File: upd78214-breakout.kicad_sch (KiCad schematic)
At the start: 26 parts, among them J1 Conn_02x17_Odd_Even, U1 upd78214-64p-qfp, X1 USB-B1HSB6

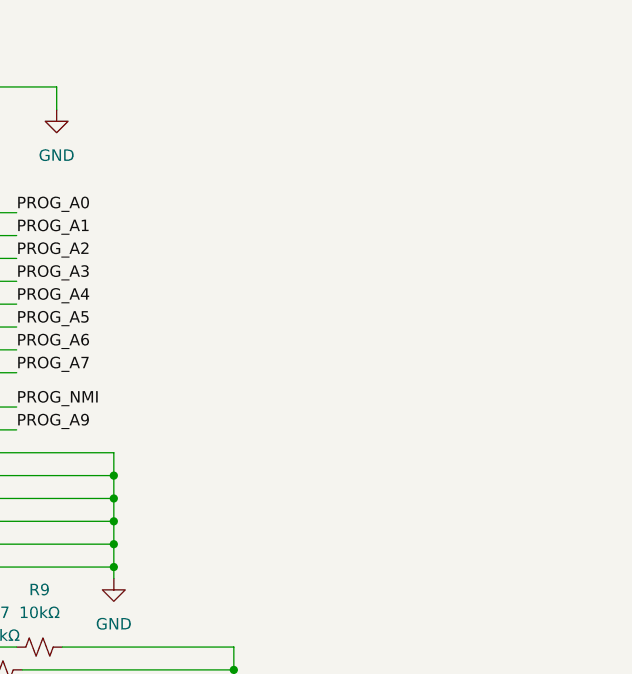
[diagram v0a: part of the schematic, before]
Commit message: 12V injection hooks
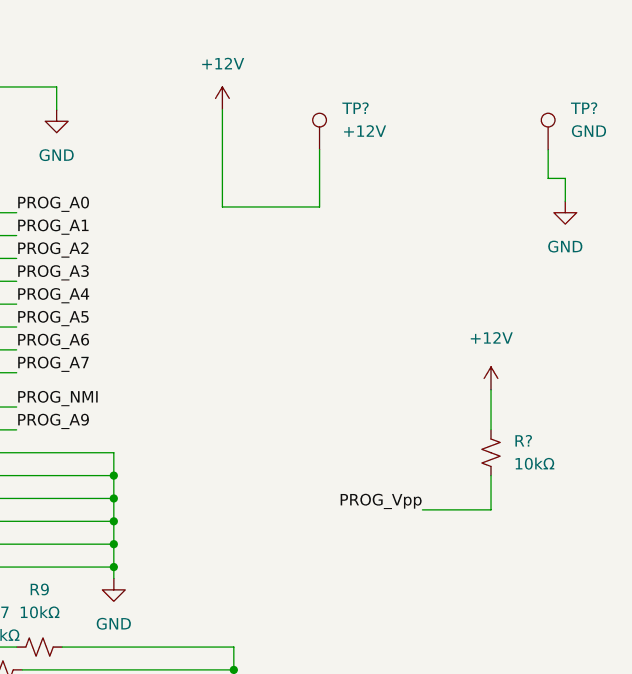
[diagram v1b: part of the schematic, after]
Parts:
- added R?: 10kΩ, Resistor_THT:R_Axial_DIN0207_L6.3mm_D2.5mm_P10.16mm_Horizontal, symbol Device:R_Small_US
- added TP?: +12V, TestPoint:TestPoint_Bridge_Pitch5.08mm_Drill0.7mm, symbol Connector:TestPoint
- added TP?: GND, TestPoint:TestPoint_Bridge_Pitch5.08mm_Drill0.7mm, symbol Connector:TestPoint
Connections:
- net GND: now also TP?.1
- net PROG_Vpp: now also R?.2
- new net +12V: R?.1, TP?.1
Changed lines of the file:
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@@
+    (stroke (width 0) (type default) (color 0 0 0 0))
+  )
+  (wire (pts (xy 163.83 64.77) (xy 163.83 68.58))
     (stroke (width 0) (type default) (color 0 0 0 0))
   )
@@
     (stroke (width 0) (type default) (color 0 0 0 0))
   )
+  (wire (pts (xy 170.18 31.75) (xy 172.085 31.75))
+    (stroke (width 0) (type default) (color 0 0 0 0))
+  )
   (wire (pts (xy 128.27 151.13) (xy 128.27 158.75))
     (stroke (width 0) (type default) (color 0 0 0 0))
@@
     (stroke (width 0) (type default) (color 0 0 0 0))
   )
+  (wire (pts (xy 170.18 28.575) (xy 170.18 31.75))
+    (stroke (width 0) (type default) (color 0 0 0 0))
+  )
+  (wire (pts (xy 144.78 34.925) (xy 144.78 28.575))
+    (stroke (width 0) (type default) (color 0 0 0 0))
+  )
   (wire (pts (xy 86.995 20.32) (xy 86.995 22.86))
     (stroke (width 0) (type default) (color 0 0 0 0))
@@
     (stroke (width 0) (type default) (color 0 0 0 0))
   )
+  (wire (pts (xy 163.83 55.245) (xy 163.83 59.69))
+    (stroke (width 0) (type default) (color 0 0 0 0))
+  )
   (wire (pts (xy 121.92 67.31) (xy 121.92 69.85))
     (stroke (width 0) (type default) (color 0 0 0 0))
@@
     (stroke (width 0) (type default) (color 0 0 0 0))
   )
+  (wire (pts (xy 133.985 24.13) (xy 133.985 34.925))
+    (stroke (width 0) (type default) (color 0 0 0 0))
+  )
   (wire (pts (xy 103.505 69.85) (xy 121.92 69.85))
     (stroke (width 0) (type default) (color 0 0 0 0))
@@
     (stroke (width 0) (type default) (color 0 0 0 0))
   )
+  (wire (pts (xy 163.83 68.58) (xy 156.21 68.58))
+    (stroke (width 0) (type default) (color 0 0 0 0))
+  )
   (wire (pts (xy 103.505 67.31) (xy 121.92 67.31))
     (stroke (width 0) (type default) (color 0 0 0 0))
@@
     (stroke (width 0) (type default) (color 0 0 0 0))
   )
+  (wire (pts (xy 133.985 34.925) (xy 144.78 34.925))
+    (stroke (width 0) (type default) (color 0 0 0 0))
+  )
   (wire (pts (xy 114.3 167.64) (xy 128.27 167.64))
     (stroke (width 0) (type default) (color 0 0 0 0))
@@
     (stroke (width 0) (type default) (color 0 0 0 0))
   )
+  (wire (pts (xy 172.085 31.75) (xy 172.085 34.29))
+    (stroke (width 0) (type default) (color 0 0 0 0))
+  )
   (wire (pts (xy 103.505 50.8) (xy 111.125 50.8))
     (stroke (width 0) (type default) (color 0 0 0 0))
@@
   )
   (label "PROG_D4" (at 38.735 104.14 180)
+    (effects (font (size 1.27 1.27)) (justify right bottom))
+  )
+  (label "PROG_Vpp" (at 156.21 68.58 180)
     (effects (font (size 1.27 1.27)) (justify right bottom))
   )
@@
     (pin "1")
     (pin "2")
+  )
+  (symbol (lib_id "power:GND") (at 172.085 34.29 0) (unit 1)
+    (in_bom yes) (on_board yes) (fields_autoplaced)
+    (property "Reference" "#PWR?" (id 0) (at 172.085 40.64 0)
+      (effects (font (size 1.27 1.27)) hide)
+    )
+    (property "Value" "GND" (id 1) (at 172.085 39.37 0))
+    (property "Footprint" "" (id 2) (at 172.085 34.29 0)
+      (effects (font (size 1.27 1.27)) hide)
+    )
+    (property "Datasheet" "" (id 3) (at 172.085 34.29 0)
+      (effects (font (size 1.27 1.27)) hide)
+    )
+    (pin "1")
   )
   (symbol (lib_id "Device:R_Small_US") (at 116.84 170.18 90) (unit 1)
@@
     (pin "1")
   )
+  (symbol (lib_id "Connector:TestPoint") (at 144.78 28.575 0) (unit 1)
+    (in_bom yes) (on_board yes) (fields_autoplaced)
+    (property "Reference" "TP?" (id 0) (at 147.32 24.0029 0)
+      (effects (font (size 1.27 1.27)) (justify left))
+    )
+    (property "Value" "+12V" (id 1) (at 147.32 26.5429 0)
+      (effects (font (size 1.27 1.27)) (justify left))
+    )
+    (property "Footprint" "TestPoint:TestPoint_Bridge_Pitch5.08mm_Drill0.7mm" (id 2) (at 149.86 28.575 0)
+      (effects (font (size 1.27 1.27)) hide)
+    )
+    (property "Datasheet" "~" (id 3) (at 149.86 28.575 0)
+      (effects (font (size 1.27 1.27)) hide)
+    )
+    (pin "1")
+  )
   (symbol (lib_id "power:GND") (at 115.57 24.13 0) (unit 1)
     (in_bom yes) (on_board yes) (fields_autoplaced)
@@
     (pin "1")
     (pin "2")
+  )
+  (symbol (lib_id "Connector:TestPoint") (at 170.18 28.575 0) (unit 1)
+    (in_bom yes) (on_board yes) (fields_autoplaced)
+    (property "Reference" "TP?" (id 0) (at 172.72 24.0029 0)
+      (effects (font (size 1.27 1.27)) (justify left))
+    )
+    (property "Value" "GND" (id 1) (at 172.72 26.5429 0)
+      (effects (font (size 1.27 1.27)) (justify left))
+    )
+    (property "Footprint" "TestPoint:TestPoint_Bridge_Pitch5.08mm_Drill0.7mm" (id 2) (at 175.26 28.575 0)
+      (effects (font (size 1.27 1.27)) hide)
+    )
+    (property "Datasheet" "~" (id 3) (at 175.26 28.575 0)
+      (effects (font (size 1.27 1.27)) hide)
+    )
+    (pin "1")
   )
   (symbol (lib_id "power:GND") (at 68.58 192.405 0) (unit 1)
@@
     )
     (property "Datasheet" "~" (id 3) (at 107.315 165.1 0)
+      (effects (font (size 1.27 1.27)) hide)
+    )
+    (pin "1")
+    (pin "2")
+  )
+  (symbol (lib_id "power:+12V") (at 133.985 24.13 0) (unit 1)
+    (in_bom yes) (on_board yes) (fields_autoplaced)
+    (property "Reference" "#PWR?" (id 0) (at 133.985 27.94 0)
+      (effects (font (size 1.27 1.27)) hide)
+    )
+    (property "Value" "+12V" (id 1) (at 133.985 19.05 0))
+    (property "Footprint" "" (id 2) (at 133.985 24.13 0)
+      (effects (font (size 1.27 1.27)) hide)
+    )
+    (property "Datasheet" "" (id 3) (at 133.985 24.13 0)
+      (effects (font (size 1.27 1.27)) hide)
+    )
+    (pin "1")
+  )
+  (symbol (lib_id "power:+12V") (at 163.83 55.245 0) (unit 1)
+    (in_bom yes) (on_board yes) (fields_autoplaced)
+    (property "Reference" "#PWR?" (id 0) (at 163.83 59.055 0)
+      (effects (font (size 1.27 1.27)) hide)
+    )
+    (property "Value" "+12V" (id 1) (at 163.83 49.53 0))
+    (property "Footprint" "" (id 2) (at 163.83 55.245 0)
+      (effects (font (size 1.27 1.27)) hide)
+    )
+    (property "Datasheet" "" (id 3) (at 163.83 55.245 0)
+      (effects (font (size 1.27 1.27)) hide)
+    )
+    (pin "1")
+  )
+  (symbol (lib_id "Device:R_Small_US") (at 163.83 62.23 0) (unit 1)
+    (in_bom yes) (on_board yes) (fields_autoplaced)
+    (property "Reference" "R?" (id 0) (at 166.37 60.9599 0)
+      (effects (font (size 1.27 1.27)) (justify left))
+    )
+    (property "Value" "10kΩ" (id 1) (at 166.37 63.4999 0)
+      (effects (font (size 1.27 1.27)) (justify left))
+    )
+    (property "Footprint" "Resistor_THT:R_Axial_DIN0207_L6.3mm_D2.5mm_P10.16mm_Horizontal" (id 2) (at 163.83 62.23 0)
+      (effects (font (size 1.27 1.27)) hide)
+    )
+    (property "Datasheet" "~" (id 3) (at 163.83 62.23 0)
       (effects (font (size 1.27 1.27)) hide)
     )
@@
       (reference "#PWR0115") (unit 1) (value "GND") (footprint "")
     )
+    (path "/4fac4605-670b-4c17-a082-ab0e08b81e09"
+      (reference "#PWR?") (unit 1) (value "GND") (footprint "")
+    )
+    (path "/ac902824-adcb-4fe8-b2b9-74384e4a02b2"
+      (reference "#PWR?") (unit 1) (value "+12V") (footprint "")
+    )
+    (path "/ae332483-4b0d-4e9d-a70d-76dbbe8c8fd5"
+      (reference "#PWR?") (unit 1) (value "+12V") (footprint "")
+    )
     (path "/ea05f697-d9aa-459a-811b-0d351998e19b"
       (reference "D1") (unit 1) (value "LED") (footprint "LED_THT:LED_D3.0mm")
@@
       (reference "R20") (unit 1) (value "10kΩ") (footprint "Resistor_THT:R_Axial_DIN0207_L6.3mm_D2.5mm_P10.16mm_Horizontal")
     )
+    (path "/af1e2ce7-906f-48cd-9500-4406b53c617e"
+      (reference "R?") (unit 1) (value "10kΩ") (footprint "Resistor_THT:R_Axial_DIN0207_L6.3mm_D2.5mm_P10.16mm_Horizontal")
+    )
     (path "/b3494da2-9112-497d-8dd3-ab62d10d763a"
       (reference "TP1") (unit 1) (value "TestPoint") (footprint "TestPoint:TestPoint_Loop_D2.50mm_Drill1.0mm")
@@
       (reference "TP2") (unit 1) (value "TestPoint") (footprint "TestPoint:TestPoint_Loop_D2.50mm_Drill1.0mm")
     )
+    (path "/84edc0cd-1fcc-4a14-8529-342659c9b8dd"
+      (reference "TP?") (unit 1) (value "+12V") (footprint "TestPoint:TestPoint_Bridge_Pitch5.08mm_Drill0.7mm")
+    )
+    (path "/98a4af96-80c6-470b-b4bb-9390c11816c7"
+      (reference "TP?") (unit 1) (value "GND") (footprint "TestPoint:TestPoint_Bridge_Pitch5.08mm_Drill0.7mm")
+    )
     (path "/69c7afce-fa24-4138-9624-1d45a5afe81a"

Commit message: V2 released
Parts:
- gave numbers to parts that had none: 3
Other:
- note added: "(Leave ~{WR} pulled-up for safety?)"
- note added: "Unsure why A9 moved in programmer mode"
- note removed: "TODO: Double check where A9 lives"
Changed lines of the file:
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@@
     (effects (font (size 1.27 1.27)) (justify left bottom))
   )
-  (text "TODO: Double check where A9 lives" (at 116.205 189.865 0)
+  (text "(Leave ~{WR} pulled-up for safety?)" (at 22.86 186.055 0)
+    (effects (font (size 1.27 1.27)) (justify left bottom))
+  )
+  (text "Unsure why A9 moved in programmer mode" (at 126.365 137.795 0)
     (effects (font (size 1.27 1.27)) (justify left bottom))
   )
@@
   (symbol (lib_id "power:GND") (at 172.085 34.29 0) (unit 1)
     (in_bom yes) (on_board yes) (fields_autoplaced)
-    (property "Reference" "#PWR?" (id 0) (at 172.085 40.64 0)
+    (property "Reference" "#PWR0116" (id 0) (at 172.085 40.64 0)
       (effects (font (size 1.27 1.27)) hide)
     )
@@
   (symbol (lib_id "Connector:TestPoint") (at 144.78 28.575 0) (unit 1)
     (in_bom yes) (on_board yes) (fields_autoplaced)
-    (property "Reference" "TP?" (id 0) (at 147.32 24.0029 0)
+    (property "Reference" "TP3" (id 0) (at 147.32 24.0029 0)
       (effects (font (size 1.27 1.27)) (justify left))
     )
@@
   (symbol (lib_id "Connector:TestPoint") (at 170.18 28.575 0) (unit 1)
     (in_bom yes) (on_board yes) (fields_autoplaced)
-    (property "Reference" "TP?" (id 0) (at 172.72 24.0029 0)
+    (property "Reference" "TP4" (id 0) (at 172.72 24.0029 0)
       (effects (font (size 1.27 1.27)) (justify left))
     )
@@
   (symbol (lib_id "power:+12V") (at 133.985 24.13 0) (unit 1)
     (in_bom yes) (on_board yes) (fields_autoplaced)
-    (property "Reference" "#PWR?" (id 0) (at 133.985 27.94 0)
+    (property "Reference" "#PWR0117" (id 0) (at 133.985 27.94 0)
       (effects (font (size 1.27 1.27)) hide)
     )
@@
   (symbol (lib_id "power:+12V") (at 163.83 55.245 0) (unit 1)
     (in_bom yes) (on_board yes) (fields_autoplaced)
-    (property "Reference" "#PWR?" (id 0) (at 163.83 59.055 0)
+    (property "Reference" "#PWR0118" (id 0) (at 163.83 59.055 0)
       (effects (font (size 1.27 1.27)) hide)
     )
@@
   (symbol (lib_id "Device:R_Small_US") (at 163.83 62.23 0) (unit 1)
     (in_bom yes) (on_board yes) (fields_autoplaced)
-    (property "Reference" "R?" (id 0) (at 166.37 60.9599 0)
+    (property "Reference" "R21" (id 0) (at 166.37 60.9599 0)
       (effects (font (size 1.27 1.27)) (justify left))
     )
@@
     )
     (path "/4fac4605-670b-4c17-a082-ab0e08b81e09"
-      (reference "#PWR?") (unit 1) (value "GND") (footprint "")
+      (reference "#PWR0116") (unit 1) (value "GND") (footprint "")
     )
     (path "/ac902824-adcb-4fe8-b2b9-74384e4a02b2"
-      (reference "#PWR?") (unit 1) (value "+12V") (footprint "")
+      (reference "#PWR0117") (unit 1) (value "+12V") (footprint "")
     )
     (path "/ae332483-4b0d-4e9d-a70d-76dbbe8c8fd5"
-      (reference "#PWR?") (unit 1) (value "+12V") (footprint "")
+      (reference "#PWR0118") (unit 1) (value "+12V") (footprint "")
     )
     (path "/ea05f697-d9aa-459a-811b-0d351998e19b"
@@
     )
     (path "/af1e2ce7-906f-48cd-9500-4406b53c617e"
-      (reference "R?") (unit 1) (value "10kΩ") (footprint "Resistor_THT:R_Axial_DIN0207_L6.3mm_D2.5mm_P10.16mm_Horizontal")
+      (reference "R21") (unit 1) (value "10kΩ") (footprint "Resistor_THT:R_Axial_DIN0207_L6.3mm_D2.5mm_P10.16mm_Horizontal")
     )
     (path "/b3494da2-9112-497d-8dd3-ab62d10d763a"
@@
     )
     (path "/84edc0cd-1fcc-4a14-8529-342659c9b8dd"
-      (reference "TP?") (unit 1) (value "+12V") (footprint "TestPoint:TestPoint_Bridge_Pitch5.08mm_Drill0.7mm")
+      (reference "TP3") (unit 1) (value "+12V") (footprint "TestPoint:TestPoint_Bridge_Pitch5.08mm_Drill0.7mm")
     )
     (path "/98a4af96-80c6-470b-b4bb-9390c11816c7"
-      (reference "TP?") (unit 1) (value "GND") (footprint "TestPoint:TestPoint_Bridge_Pitch5.08mm_Drill0.7mm")
+      (reference "TP4") (unit 1) (value "GND") (footprint "TestPoint:TestPoint_Bridge_Pitch5.08mm_Drill0.7mm")
     )
     (path "/69c7afce-fa24-4138-9624-1d45a5afe81a"
